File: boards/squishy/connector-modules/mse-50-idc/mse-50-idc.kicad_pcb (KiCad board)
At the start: 6 copper layers, 75 x 34 mm, 18 parts, among them J1 SCSI PHY Mezz, J2 IDC, J3 Conn_01x04, U1 M24C02-RMC

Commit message: squishy: connectors: updated the KiKit tab footprints on the mse-50-idc connector
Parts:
- moved REF** 0.30 mm to (110.0, 131.0)
- moved REF** 0.30 mm to (110.0, 115.0)
- moved REF** 0.25 mm to (121.0, 106.0)
- moved REF** 0.25 mm to (185.0, 131.0)
- moved REF** 0.25 mm to (174.0, 140.0)
- moved REF** 0.25 mm to (174.0, 106.0)
- moved REF** 0.25 mm to (185.0, 115.0)
- moved REF** 0.25 mm to (121.0, 140.0)

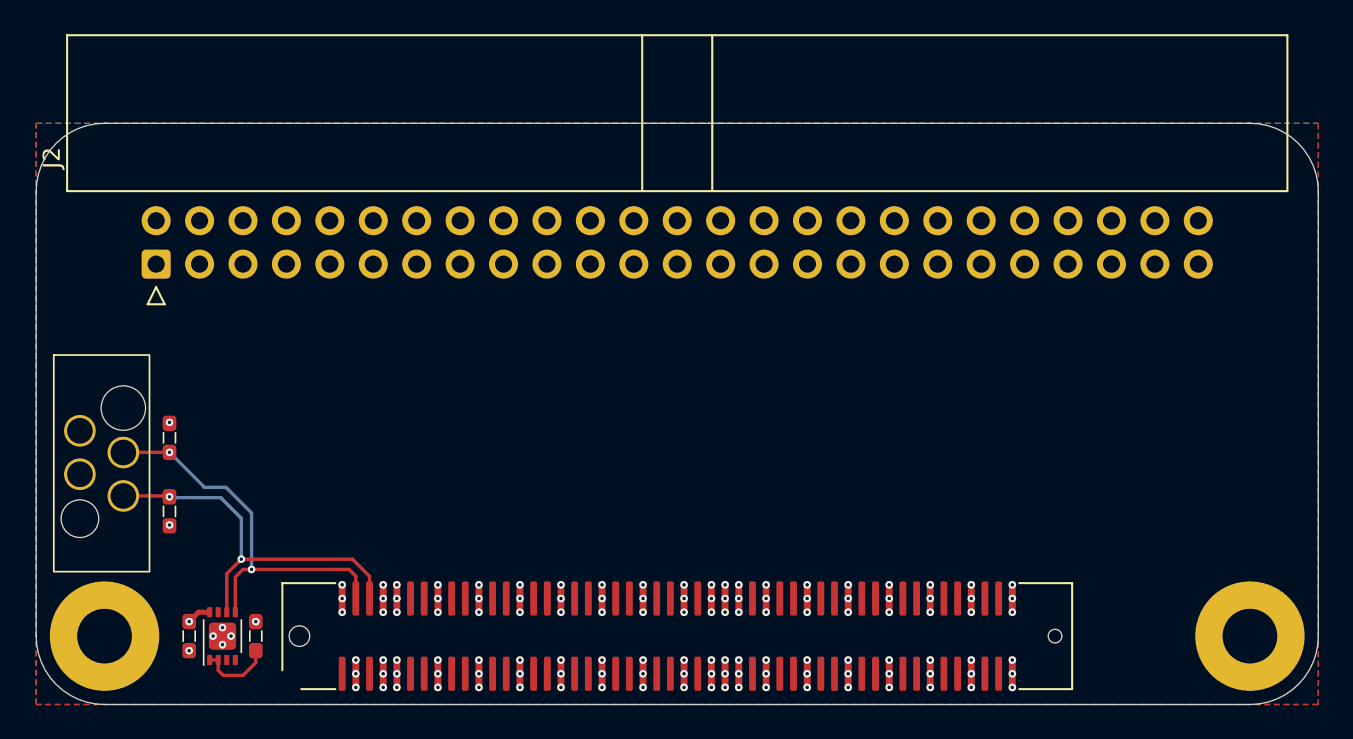
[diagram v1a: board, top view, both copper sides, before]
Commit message: squishy: connectors: routed the mse-50-idc board
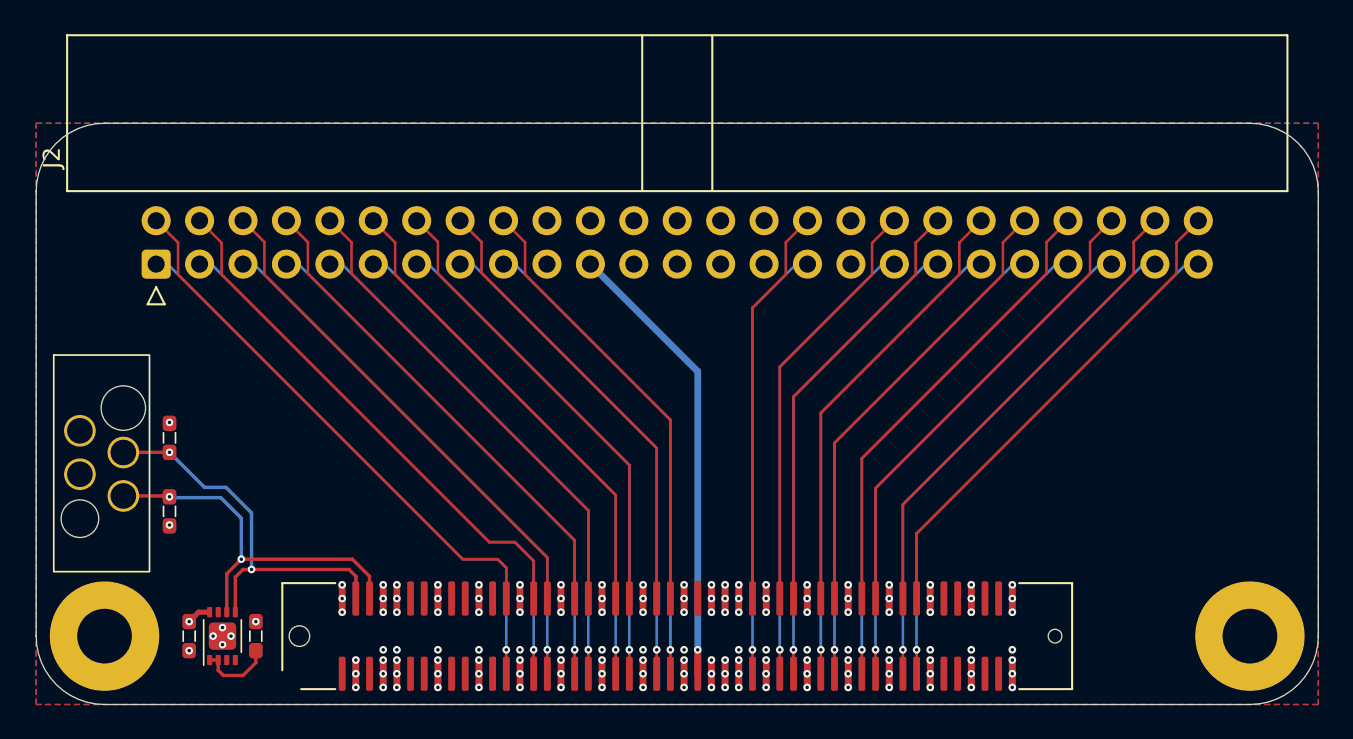
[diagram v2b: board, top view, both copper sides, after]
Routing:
- net /CON.DB0+: track 0.00 -> 34.0 mm, vias 0 -> 1
- net /CON.DB1+: track 0.00 -> 33.3 mm, vias 0 -> 1
- net /CON.DB0-: track 0.00 -> 31.8 mm
- net /CON.DB2+: track 0.00 -> 31.7 mm, vias 0 -> 1
- net /CON.DB3+: track 0.00 -> 31.4 mm, vias 0 -> 1
- net /CON.I/O+: track 0.00 -> 31.2 mm, vias 0 -> 1
- net /CON.DB1-: track 0.00 -> 31.1 mm
- net /CON.DB4+: track 0.00 -> 30.6 mm, vias 0 -> 1
- net /CON.REQ+: track 0.00 -> 30.5 mm, vias 0 -> 1
- net /CON.DB5+: track 0.00 -> 30.2 mm, vias 0 -> 1
- net /CON.C/D+: track 0.00 -> 30.1 mm, vias 0 -> 1
- net /CON.DB6+: track 0.00 -> 29.5 mm, vias 0 -> 1
- net /CON.DB2-: track 0.00 -> 29.5 mm
- net /CON.SEL+: track 0.00 -> 29.4 mm, vias 0 -> 1
- net /CON.DB7+: track 0.00 -> 29.2 mm, vias 0 -> 1
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
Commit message: squishy: connectors: length-matched mse-50-idc
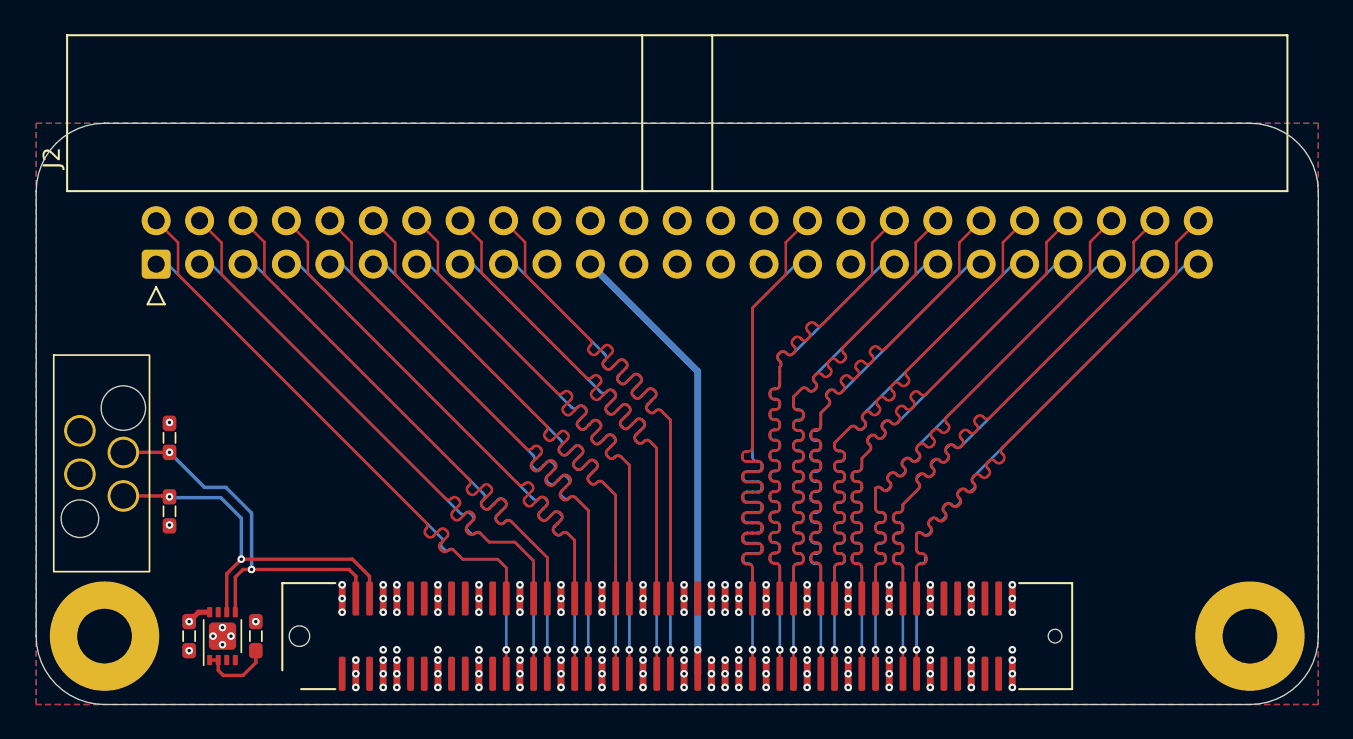
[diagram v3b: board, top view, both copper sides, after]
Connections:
- net /CON.DP12+ renamed /CON.DB12+
- net /CON.DP12- renamed /CON.DB12-
- net /CON.DP14+ renamed /CON.DB14+
- net /CON.DP14- renamed /CON.DB14-
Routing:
- net /CON.ATN-: track 23.4 -> 33.8 mm
- net /CON.BSY-: track 24.9 -> 33.6 mm
- net /CON.ATN+: track 25.7 -> 34.2 mm
- net /CON.ACK-: track 25.6 -> 33.6 mm
- net /CON.DP0-: track 26.1 -> 33.8 mm
- net /CON.RST-: track 26.0 -> 33.6 mm
- net /CON.DB7-: track 26.9 -> 33.9 mm
- net /CON.MSG-: track 26.7 -> 33.7 mm
- net /CON.BSY+: track 27.1 -> 34.0 mm
- net /CON.DB6-: track 27.3 -> 33.9 mm
- net /CON.SEL-: track 27.1 -> 33.7 mm
- net /CON.ACK+: track 27.9 -> 34.1 mm
- net /CON.C/D-: track 27.8 -> 33.7 mm
- net /CON.DB5-: track 28.0 -> 33.9 mm
- net /CON.DP0+: track 28.4 -> 34.3 mm
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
